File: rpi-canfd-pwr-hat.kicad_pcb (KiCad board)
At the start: 4 copper layers, 65 x 56 mm, 90 parts, among them J1 Conn_01x02, J2 Conn_01x04_Pin, J3 Raspberry_Pi, J4 Conn_01x02, J5 Conn_01x02, U1 XC6206P332MR, U10 SN74LV1T125DBV, U11 SN74LV1T125DBV, U12 SN74LV1T125DBV, U13 SN74LV1T125DBV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

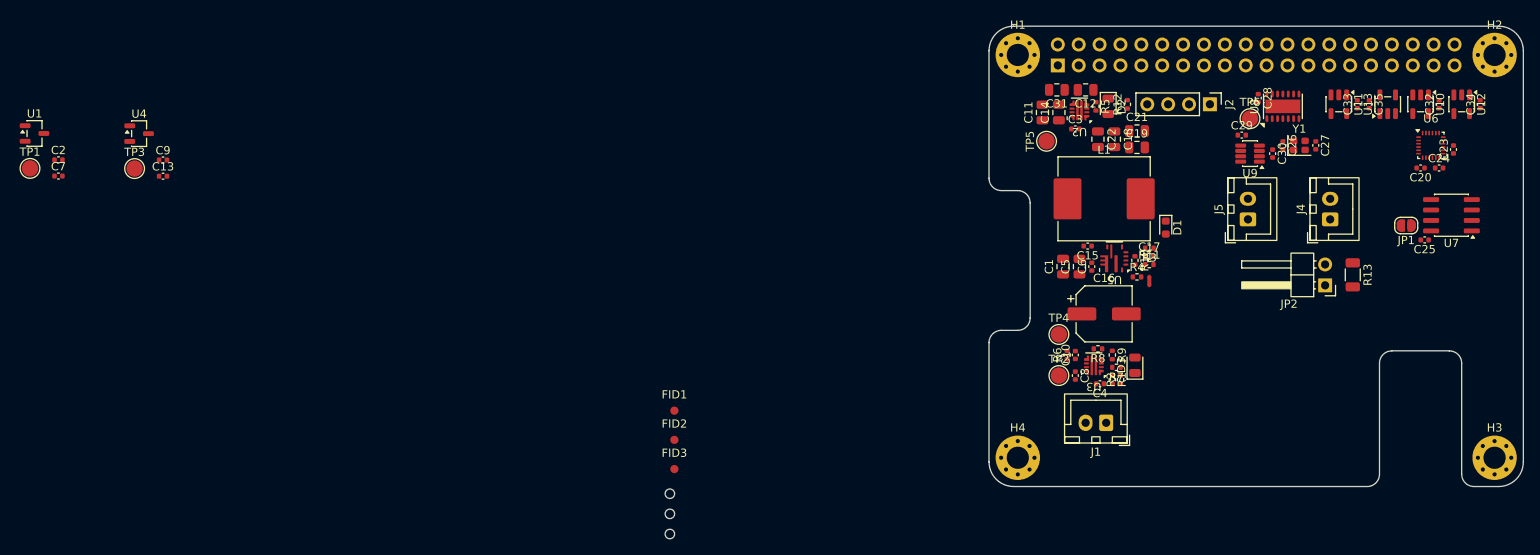
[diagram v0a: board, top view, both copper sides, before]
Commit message: pcb: update board outline
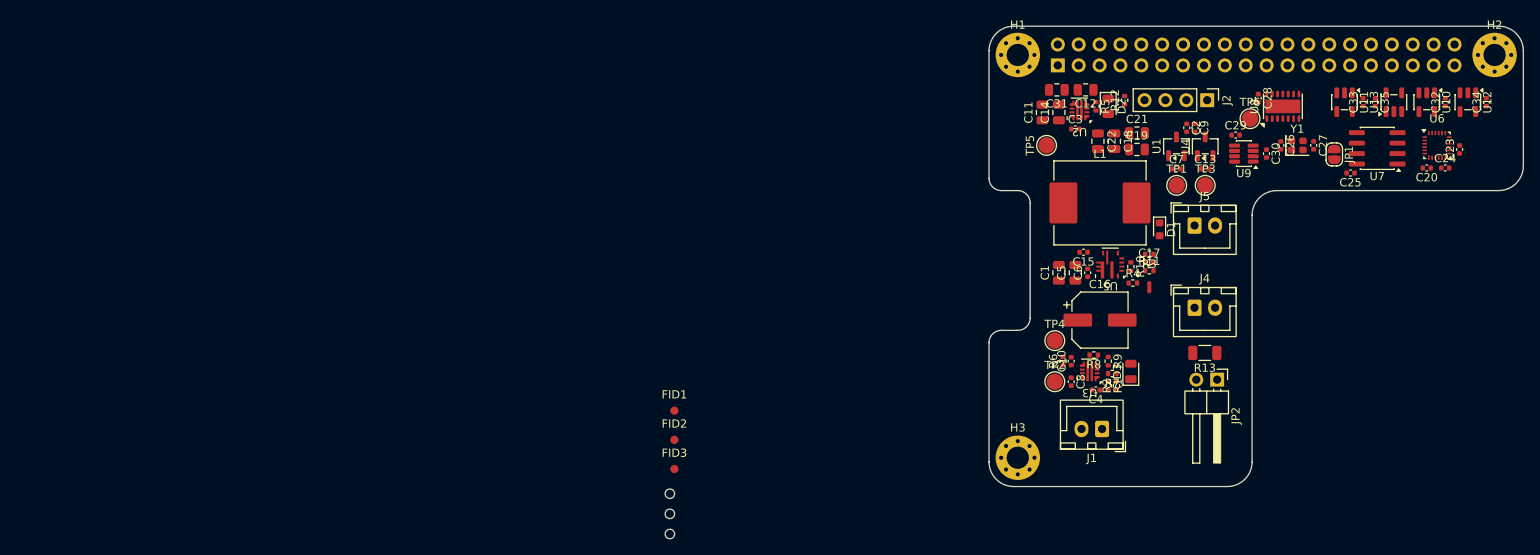
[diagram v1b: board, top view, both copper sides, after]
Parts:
- removed the H3 at (211.5, 122.5)
- moved TP1 139.5 mm to (172.8, 89.4)
- moved U1 138.9 mm to (172.8, 84.6), turned to 90 degrees
- moved C2 137.3 mm to (174.1, 82.4), turned to -90 degrees
- moved C7 136.0 mm to (172.8, 87.4)
- moved TP3 130.3 mm to (176.3, 89.4)
- moved U4 129.7 mm to (176.3, 84.6), turned to 90 degrees
- moved C13 126.8 mm to (176.3, 87.4)
- moved C9 125.6 mm to (175.1, 82.4), turned to -90 degrees
- moved R13 20.4 mm to (176.2, 109.8), turned to 180 degrees
- moved J4 19.7 mm to (175.0, 104.2), turned to 0 degrees
- moved JP2 17.4 mm to (177.8, 113.0), turned to -90 degrees
- moved JP1 12.3 mm to (192.0, 85.6), turned to -90 degrees
- moved C25 12.2 mm to (194.0, 87.9)
- moved U7 12.2 mm to (197.2, 84.9)
- moved J5 6.54 mm to (175.0, 94.2), turned to 0 degrees
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- renumbered H4 to H3
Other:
- outline, holes or cut-outs redrawn

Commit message: pcb: final board layout
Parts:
- moved H6 109.3 mm to (212.0, 87.0)
- moved FID2 104.8 mm to (210.0, 84.0)
- moved FID3 58.3 mm to (170.0, 121.0)
- moved H5 57.8 mm to (153.0, 87.0)
- moved FID1 54.6 mm to (153.0, 81.0)
- moved H7 44.4 mm to (153.0, 117.0)
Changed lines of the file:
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@@
 	(footprint "MountingHole:ToolingHole_1.152mm"
 		(layer "F.Cu")
-		(at 111.175 129.325)
+		(at 212 87)
 		(descr "Tooling Hole 1.152mm, 1.3mm solder mask, JLCPCB specification, https://jlcpcb.com/help/article/How-to-add-tooling-holes-for-PCB-assembly-order")
 		(tags "mounting")
@@
 			(polygon
 				(pts
-					(xy 111.875 129.325) (xy 111.854659 129.157479) (xy 111.794819 128.999694) (xy 111.698958 128.860814)
-					(xy 111.572645 128.748911) (xy 111.423223 128.670489) (xy 111.259376 128.630104) (xy 111.090624 128.630104)
-					(xy 110.926777 128.670489) (xy 110.777355 128.748911) (xy 110.651042 128.860814) (xy 110.555181 128.999694)
-					(xy 110.495341 129.157479) (xy 110.475 129.325) (xy 110.495341 129.492521) (xy 110.555181 129.650306)
-					(xy 110.651042 129.789186) (xy 110.777355 129.901089) (xy 110.926777 129.979511) (xy 111.090624 130.019896)
-					(xy 111.259376 130.019896) (xy 111.423223 129.979511) (xy 111.572645 129.901089) (xy 111.698958 129.789186)
-					(xy 111.794819 129.650306) (xy 111.854659 129.492521)
+					(xy 212.7 87) (xy 212.679659 86.832479) (xy 212.619819 86.674694) (xy 212.523958 86.535814) (xy 212.397645 86.423911)
+					(xy 212.248223 86.345489) (xy 212.084376 86.305104) (xy 211.915624 86.305104) (xy 211.751777 86.345489)
+					(xy 211.602355 86.423911) (xy 211.476042 86.535814) (xy 211.380181 86.674694) (xy 211.320341 86.832479)
+					(xy 211.3 87) (xy 211.320341 87.167521) (xy 211.380181 87.325306) (xy 211.476042 87.464186) (xy 211.602355 87.576089)
+					(xy 211.751777 87.654511) (xy 211.915624 87.694896) (xy 212.084376 87.694896) (xy 212.248223 87.654511)
+					(xy 212.397645 87.576089) (xy 212.523958 87.464186) (xy 212.619819 87.325306) (xy 212.679659 87.167521)
 				)
 			)
@@
 	(footprint "MountingHole:ToolingHole_1.152mm"
 		(layer "F.Cu")
-		(at 111.175 131.775)
+		(at 153 117)
 		(descr "Tooling Hole 1.152mm, 1.3mm solder mask, JLCPCB specification, https://jlcpcb.com/help/article/How-to-add-tooling-holes-for-PCB-assembly-order")
 		(tags "mounting")
@@
 			(polygon
 				(pts
-					(xy 111.875 131.775) (xy 111.854659 131.607479) (xy 111.794819 131.449694) (xy 111.698958 131.310814)
-					(xy 111.572645 131.198911) (xy 111.423223 131.120489) (xy 111.259376 131.080104) (xy 111.090624 131.080104)
-					(xy 110.926777 131.120489) (xy 110.777355 131.198911) (xy 110.651042 131.310814) (xy 110.555181 131.449694)
-					(xy 110.495341 131.607479) (xy 110.475 131.775) (xy 110.495341 131.942521) (xy 110.555181 132.100306)
-					(xy 110.651042 132.239186) (xy 110.777355 132.351089) (xy 110.926777 132.429511) (xy 111.090624 132.469896)
-					(xy 111.259376 132.469896) (xy 111.423223 132.429511) (xy 111.572645 132.351089) (xy 111.698958 132.239186)
-					(xy 111.794819 132.100306) (xy 111.854659 131.942521)
+					(xy 153.7 117) (xy 153.679659 116.832479) (xy 153.619819 116.674694) (xy 153.523958 116.535814)
+					(xy 153.397645 116.423911) (xy 153.248223 116.345489) (xy 153.084376 116.305104) (xy 152.915624 116.305104)
+					(xy 152.751777 116.345489) (xy 152.602355 116.423911) (xy 152.476042 116.535814) (xy 152.380181 116.674694)
+					(xy 152.320341 116.832479) (xy 152.3 117) (xy 152.320341 117.167521) (xy 152.380181 117.325306)
+					(xy 152.476042 117.464186) (xy 152.602355 117.576089) (xy 152.751777 117.654511) (xy 152.915624 117.694896)
+					(xy 153.084376 117.694896) (xy 153.248223 117.654511) (xy 153.397645 117.576089) (xy 153.523958 117.464186)
+					(xy 153.619819 117.325306) (xy 153.679659 117.167521)
 				)
 			)
@@
 	(footprint "Fiducial:Fiducial_1mm_Mask2mm"
 		(layer "F.Cu")
-		(at 111.725 116.775)
+		(at 153 81)
 		(descr "Fiducial, circular marking, 1mm bare copper, 2mm soldermask opening (Level A)")
 		(tags "fiducial")
@@
 	(footprint "Fiducial:Fiducial_1mm_Mask2mm"
 		(layer "F.Cu")
-		(at 111.725 120.325)
+		(at 210 84)
 		(descr "Fiducial, circular marking, 1mm bare copper, 2mm soldermask opening (Level A)")
 		(tags "fiducial")
@@
 	(footprint "Fiducial:Fiducial_1mm_Mask2mm"
 		(layer "F.Cu")
-		(at 111.725 123.875)
+		(at 170 121)
 		(descr "Fiducial, circular marking, 1mm bare copper, 2mm soldermask opening (Level A)")
 		(tags "fiducial")
@@
 	(footprint "MountingHole:ToolingHole_1.152mm"
 		(layer "F.Cu")
-		(at 111.175 126.875)
+		(at 153 87)
 		(descr "Tooling Hole 1.152mm, 1.3mm solder mask, JLCPCB specification, https://jlcpcb.com/help/article/How-to-add-tooling-holes-for-PCB-assembly-order")
 		(tags "mounting")
@@
 			(polygon
 				(pts
-					(xy 111.875 126.875) (xy 111.854659 126.707479) (xy 111.794819 126.549694) (xy 111.698958 126.410814)
-					(xy 111.572645 126.298911) (xy 111.423223 126.220489) (xy 111.259376 126.180104) (xy 111.090624 126.180104)
-					(xy 110.926777 126.220489) (xy 110.777355 126.298911) (xy 110.651042 126.410814) (xy 110.555181 126.549694)
-					(xy 110.495341 126.707479) (xy 110.475 126.875) (xy 110.495341 127.042521) (xy 110.555181 127.200306)
-					(xy 110.651042 127.339186) (xy 110.777355 127.451089) (xy 110.926777 127.529511) (xy 111.090624 127.569896)
-					(xy 111.259376 127.569896) (xy 111.423223 127.529511) (xy 111.572645 127.451089) (xy 111.698958 127.339186)
-					(xy 111.794819 127.200306) (xy 111.854659 127.042521)
+					(xy 153.7 87) (xy 153.679659 86.832479) (xy 153.619819 86.674694) (xy 153.523958 86.535814) (xy 153.397645 86.423911)
+					(xy 153.248223 86.345489) (xy 153.084376 86.305104) (xy 152.915624 86.305104) (xy 152.751777 86.345489)
+					(xy 152.602355 86.423911) (xy 152.476042 86.535814) (xy 152.380181 86.674694) (xy 152.320341 86.832479)
+					(xy 152.3 87) (xy 152.320341 87.167521) (xy 152.380181 87.325306) (xy 152.476042 87.464186) (xy 152.602355 87.576089)
+					(xy 152.751777 87.654511) (xy 152.915624 87.694896) (xy 153.084376 87.694896) (xy 153.248223 87.654511)
+					(xy 153.397645 87.576089) (xy 153.523958 87.464186) (xy 153.619819 87.325306) (xy 153.679659 87.167521)
 				)
 			)

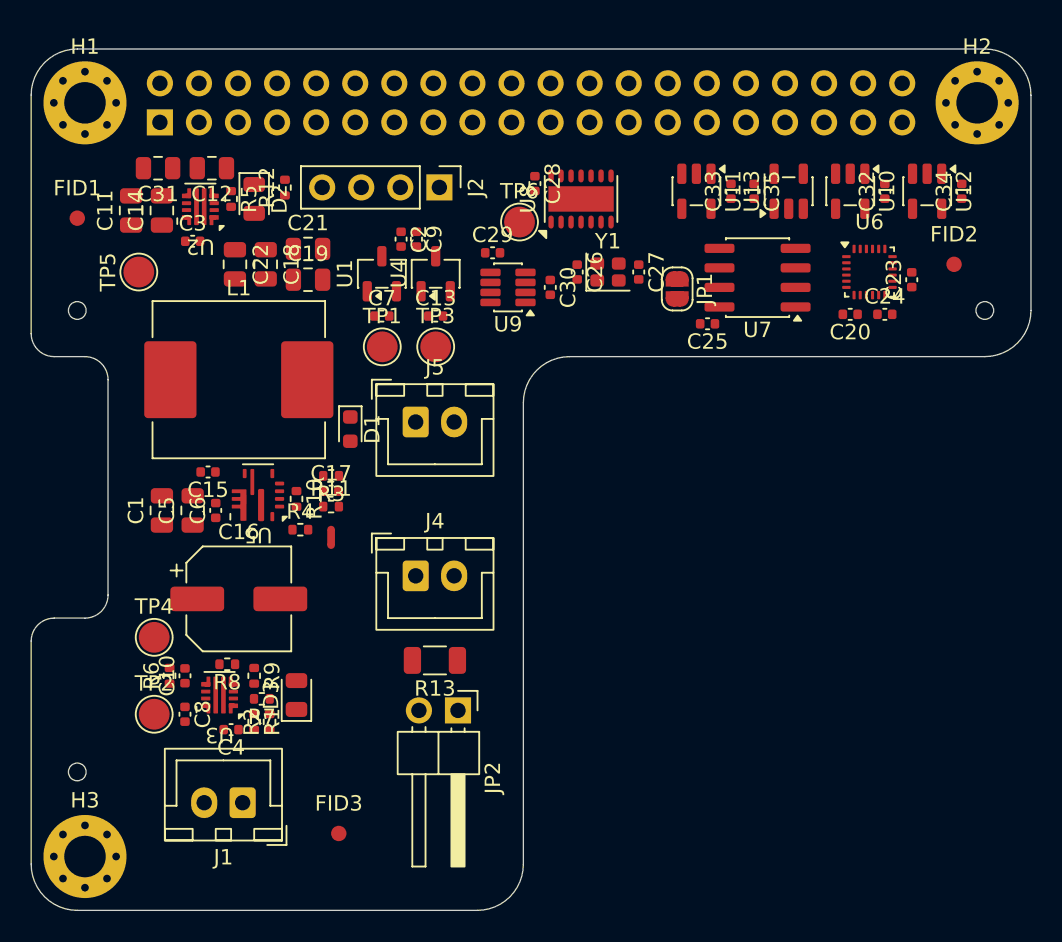
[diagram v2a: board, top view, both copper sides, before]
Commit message: pcb: add gnd planes
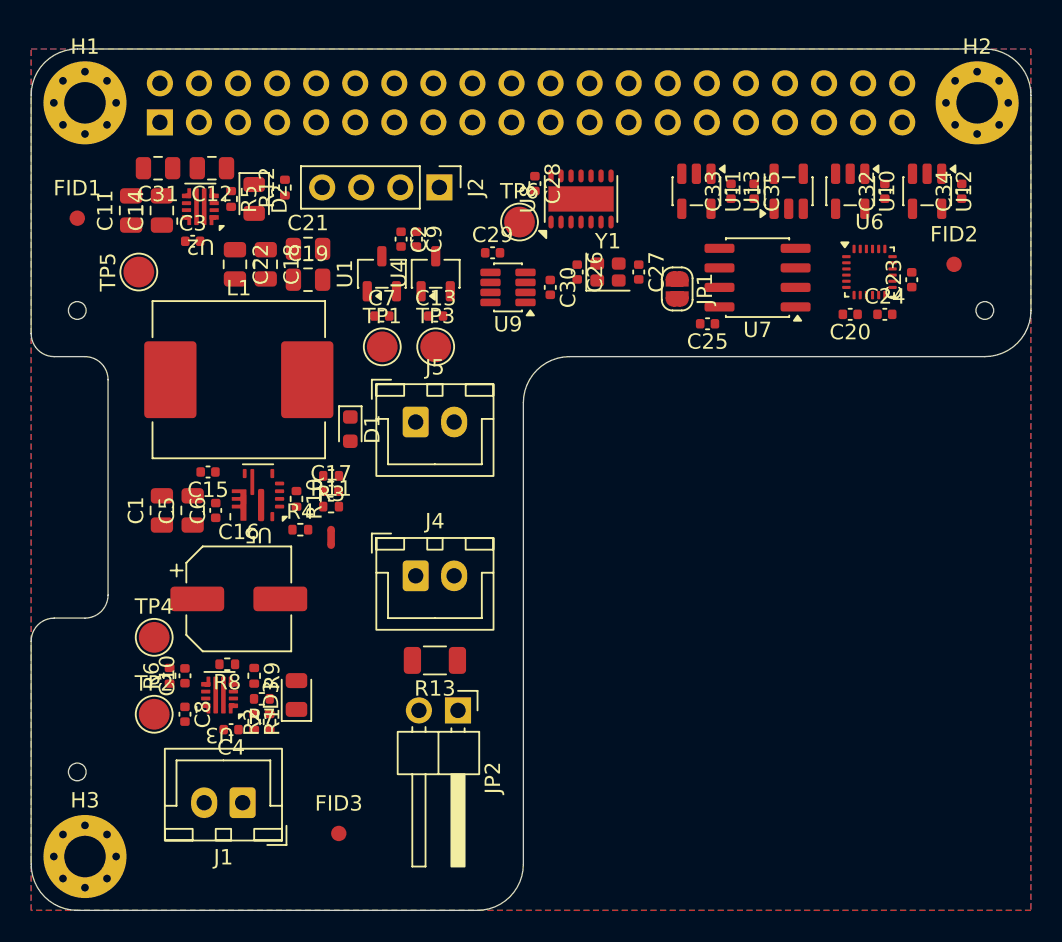
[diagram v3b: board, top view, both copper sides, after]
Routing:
- added copper zone on B.Cu, net GND
- added copper zone on F.Cu, net GND
- added copper zone on In1.Cu, net GND
- added copper zone on In2.Cu, net GND
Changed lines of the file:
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@@
+	)
+	(zone
+		(net "GND")
+		(layers "F.Cu" "B.Cu" "In1.Cu" "In2.Cu")
+		(hatch edge 0.5)
+		(priority 1)
+		(connect_pads
+			(clearance 0.2)
+		)
+		(min_thickness 0.15)
+		(fill yes
+			(thermal_gap 0.35)
+			(thermal_bridge_width 0.35)
+			(island_removal_mode 0)
+		)
+		(polygon
+			(pts
+				(xy 150 70) (xy 215 70) (xy 215 126) (xy 150 126)
+			)
+		)
 	)
 	(zone
@@
 		)
 		(min_thickness 0.15)
-		(fill
+		(fill yes
 			(thermal_gap 0.35)
 			(thermal_bridge_width 0.35)

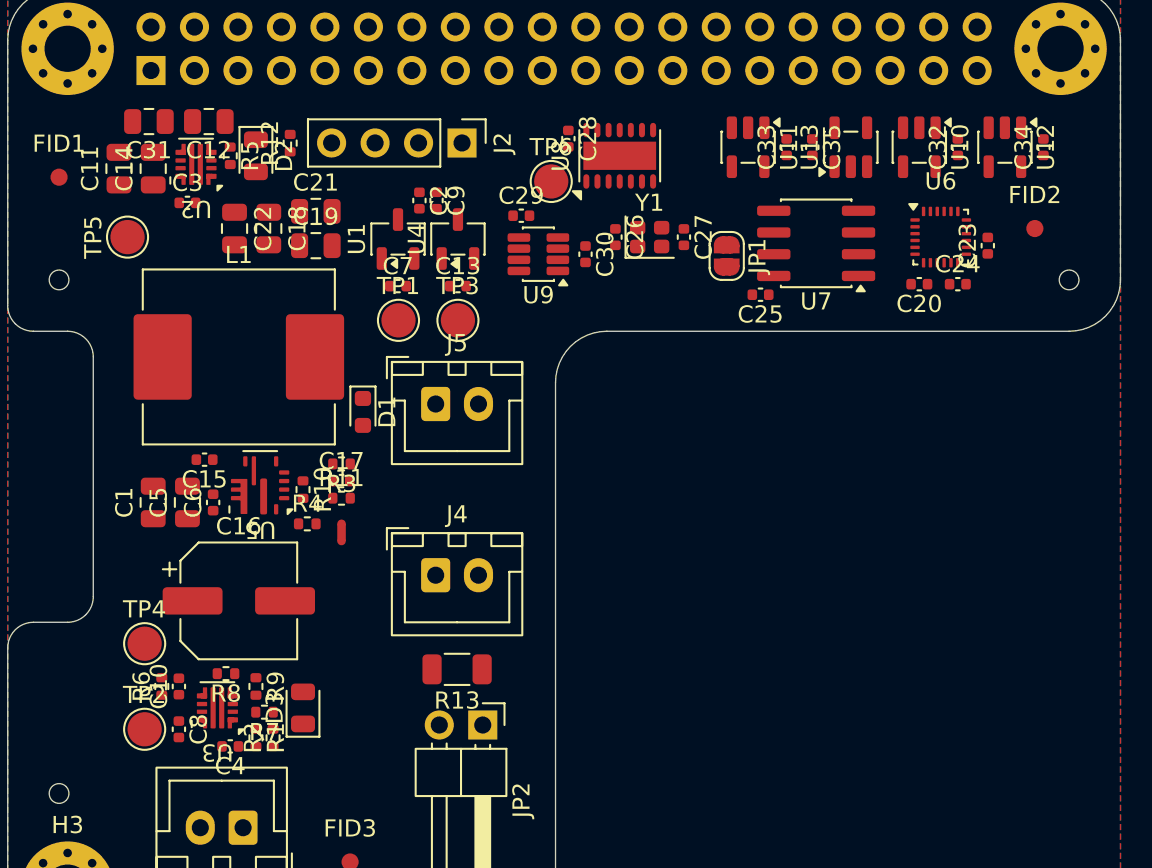
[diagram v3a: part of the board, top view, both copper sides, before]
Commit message: pcb: add gnd vias
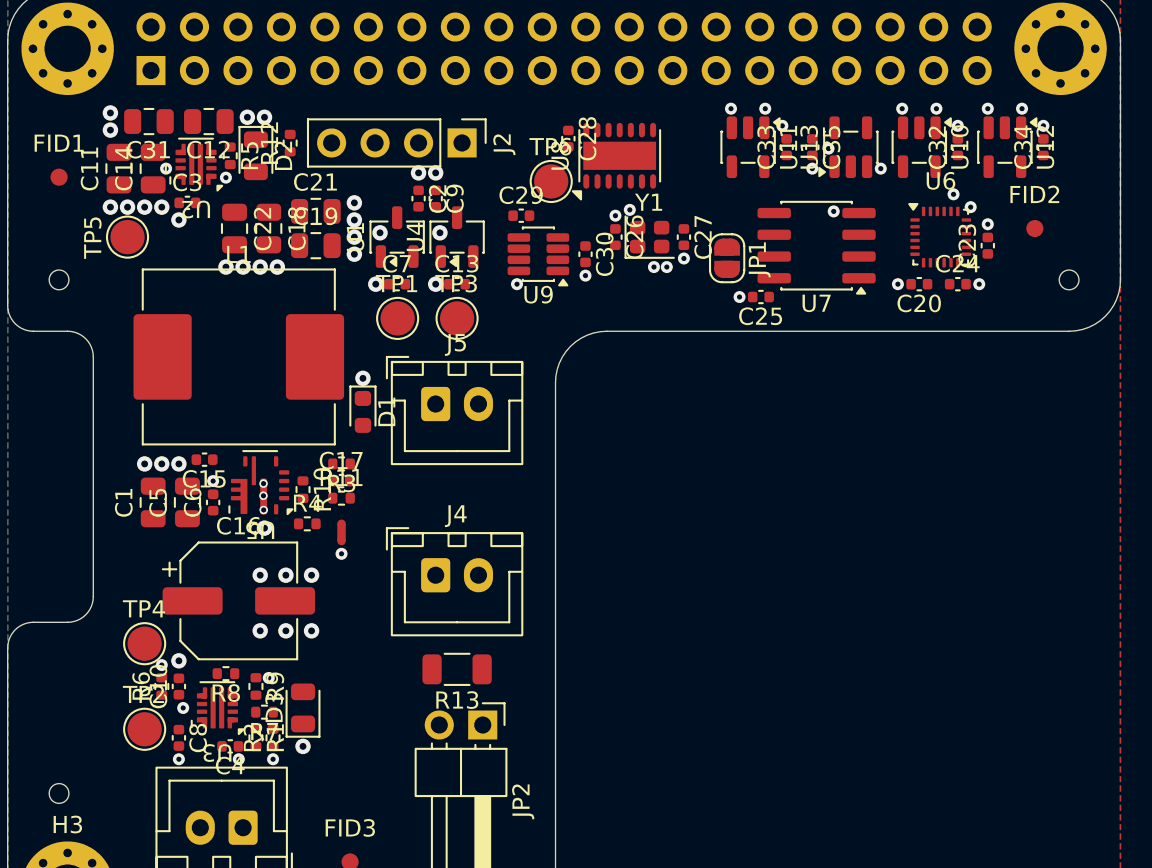
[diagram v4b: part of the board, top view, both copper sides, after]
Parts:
- moved C8 0.50 mm to (160.0, 113.8)
- moved C25 0.14 mm to (194.0, 88.0)
- moved JP1 0.14 mm to (192.0, 85.7)
- moved U7 0.14 mm to (197.2, 85.0)
- moved C13 0.12 mm to (176.2, 87.2)
- moved C2 0.12 mm to (174.0, 82.2)
- moved C7 0.12 mm to (172.8, 87.2)
- moved C9 0.12 mm to (175.0, 82.2)
- moved TP3 0.12 mm to (176.2, 89.2)
- moved U1 0.12 mm to (172.8, 84.5)
- moved U4 0.12 mm to (176.2, 84.5)
- moved TP1 0.12 mm to (172.8, 89.2)
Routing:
- net GND: vias 0 -> 75
